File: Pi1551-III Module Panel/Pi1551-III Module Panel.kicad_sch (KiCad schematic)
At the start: 15 parts, among them IC1 OLED, J1 Module Panel, M1 Mounting_Pin, M2 Mounting_Pin, M3 Mounting_Pin, M4 Mounting_Pin, SW1 BACK, SW2 INSERT

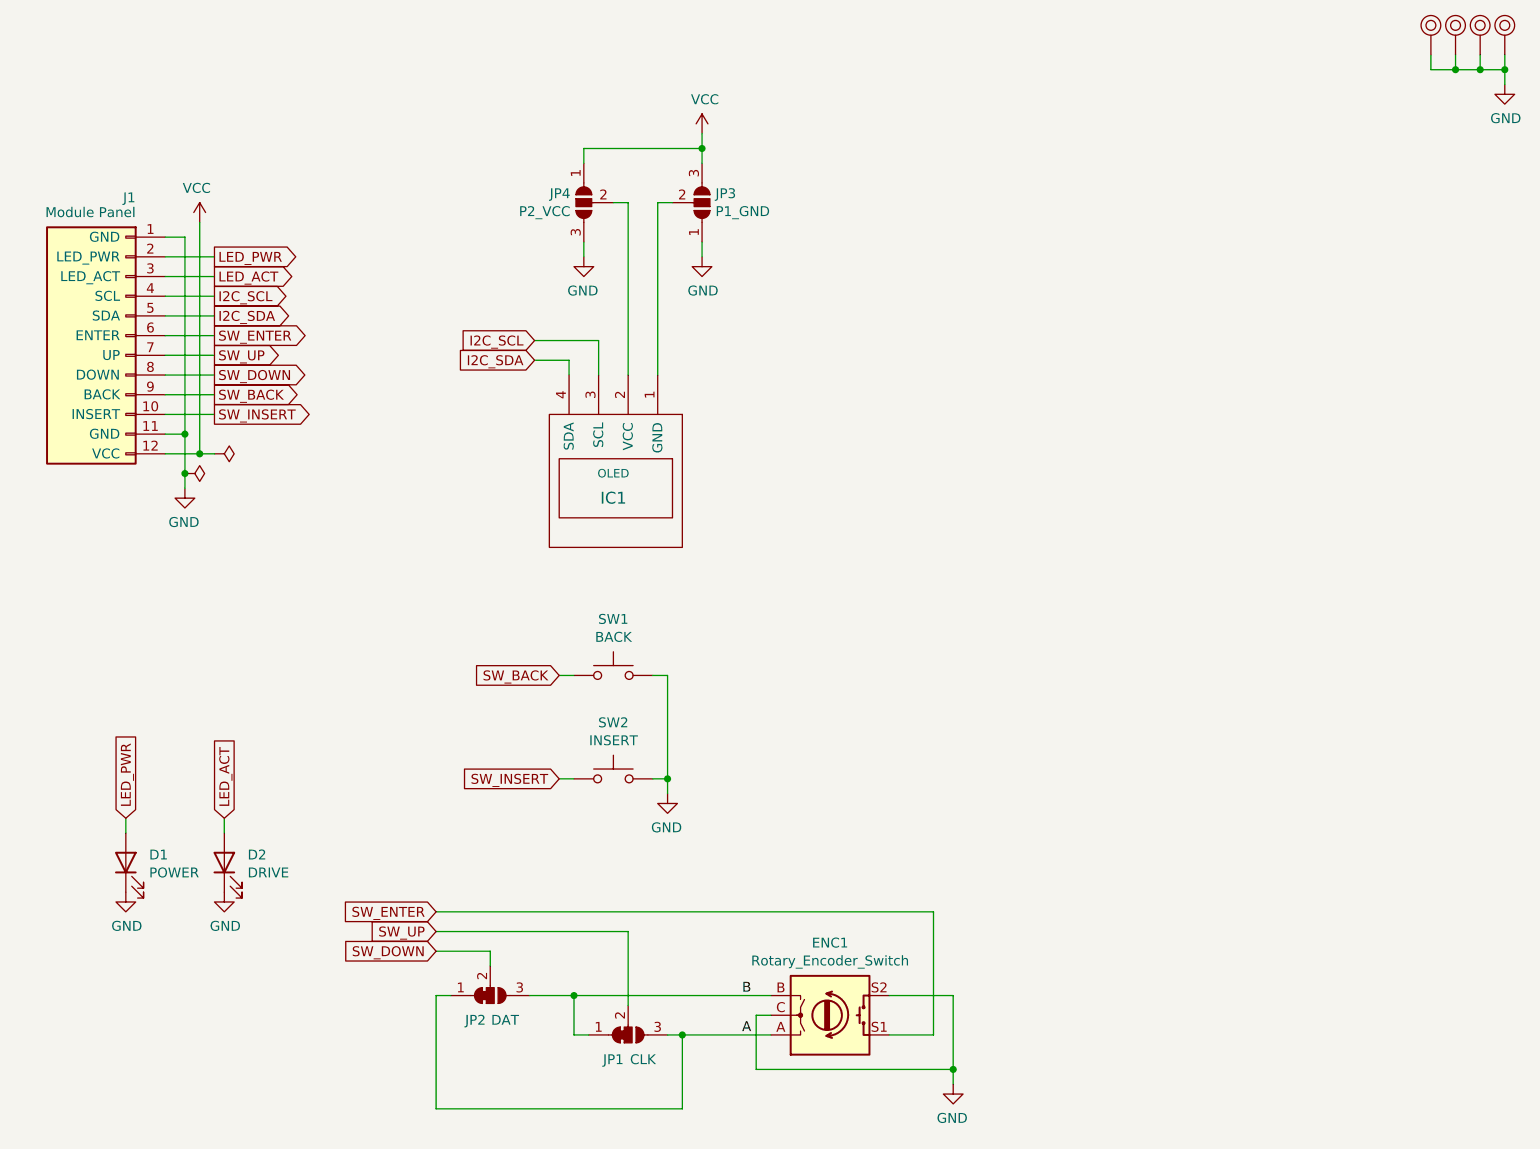
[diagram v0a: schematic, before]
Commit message: PI1551 branding and Microgramma font labels
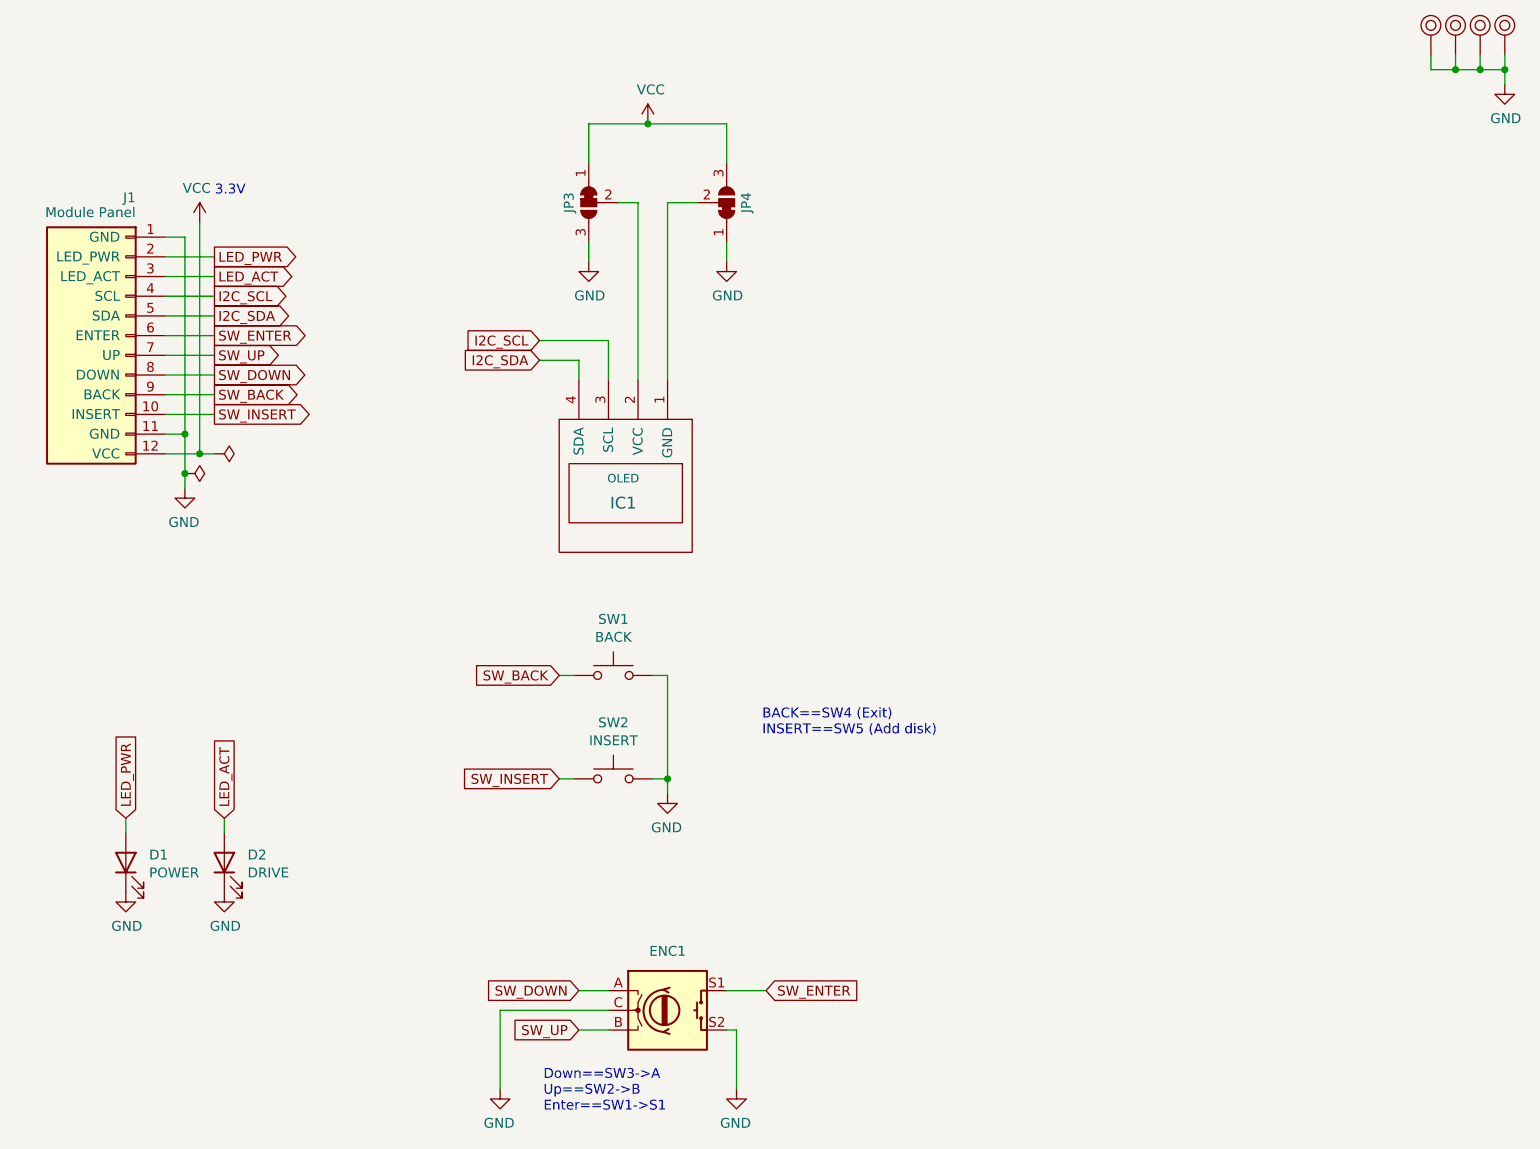
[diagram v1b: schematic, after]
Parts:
- removed ENC1: Rotary_Encoder_Switch, Rotary_Encoder:RotaryEncoder_Alps_EC11E-Switch_Vertical_H20mm, symbol Device:Rotary_Encoder_Switch
- removed JP1: CLK, Jumper:SolderJumper-3_P1.3mm_Open_Pad1.0x1.5mm, symbol Jumper:SolderJumper_3_Bridged12
- removed JP2: DAT, Jumper:SolderJumper-3_P1.3mm_Open_Pad1.0x1.5mm, symbol Jumper:SolderJumper_3_Bridged12
- removed JP3: P1_GND, Jumper:SolderJumper-3_P1.3mm_Open_Pad1.0x1.5mm, symbol I2C_OLED:PowerSelect
- removed JP4: P2_VCC, Jumper:SolderJumper-3_P1.3mm_Open_Pad1.0x1.5mm, symbol I2C_OLED:PowerSelect
- added ENC1: RotaryEncoder_Switch, Rotary_Encoder:RotaryEncoder_Alps_EC11E-Switch_Vertical_H20mm_CircularMountingHoles, symbol Device:RotaryEncoder_Switch
- added JP3, JP4: SolderJumper_3_Bridged12, Jumper:SolderJumper-3_P1.3mm_Bridged12_RoundedPad1.0x1.5mm_NumberLabels, symbol Jumper:SolderJumper_3_Bridged12
- D1, D2, IC1, J1, SW1, SW2: now left out of the parts list
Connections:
- net GND: now also ENC1.C, ENC1.S2, JP3.3 (B), JP4.1 (A)
- net SW_DOWN: now also ENC1.A
- net SW_ENTER: now also ENC1.S1
- net SW_UP: now also ENC1.B
- net VCC: now also JP3.1 (A), JP4.3 (B)
- net at IC1.2 (VCC): now also JP3.2 (C)
- net at IC1.1 (GND): now also JP4.2 (C)
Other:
- note added: "3.3V"
- note added: "BACK==SW4 (Exit) INSERT==SW5 (Add disk)"
- note added: "Down==SW3->A Up==SW2->B Enter==SW1->S1"
- moved on the sheet: IC1

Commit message: gerber files for fabrication
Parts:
- M1, M2, M3, M4: now left out of the parts list
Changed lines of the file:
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@@
 		(unit 1)
 		(exclude_from_sim no)
-		(in_bom yes)
+		(in_bom no)
 		(on_board yes)
 		(dnp no)
@@
 		(unit 1)
 		(exclude_from_sim no)
-		(in_bom yes)
+		(in_bom no)
 		(on_board yes)
 		(dnp no)
@@
 		(unit 1)
 		(exclude_from_sim no)
-		(in_bom yes)
+		(in_bom no)
 		(on_board yes)
 		(dnp no)
@@
 		(unit 1)
 		(exclude_from_sim no)
-		(in_bom yes)
+		(in_bom no)
 		(on_board yes)
 		(dnp no)

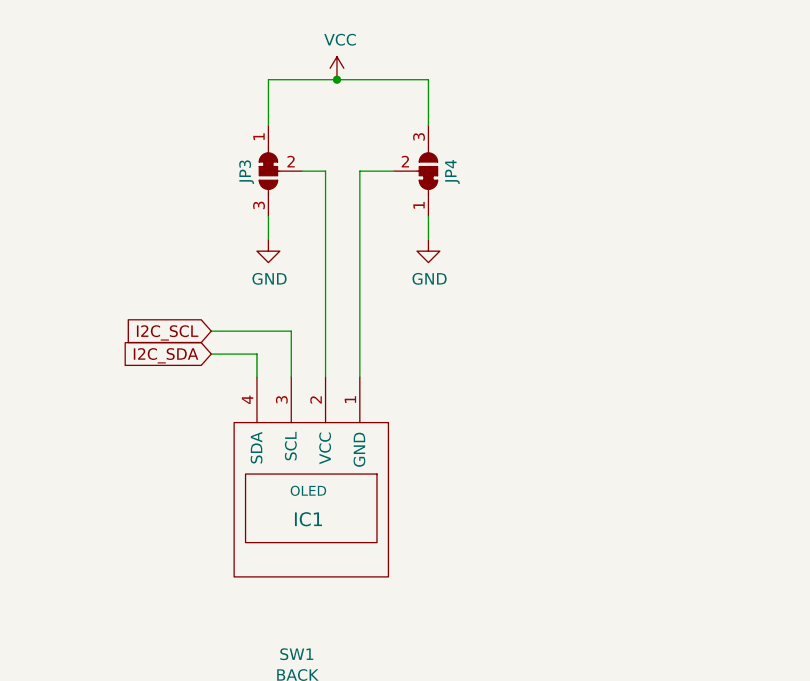
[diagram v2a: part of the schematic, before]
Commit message: change jumpers to be open - it's too difficult to cut them once panel is soldered in
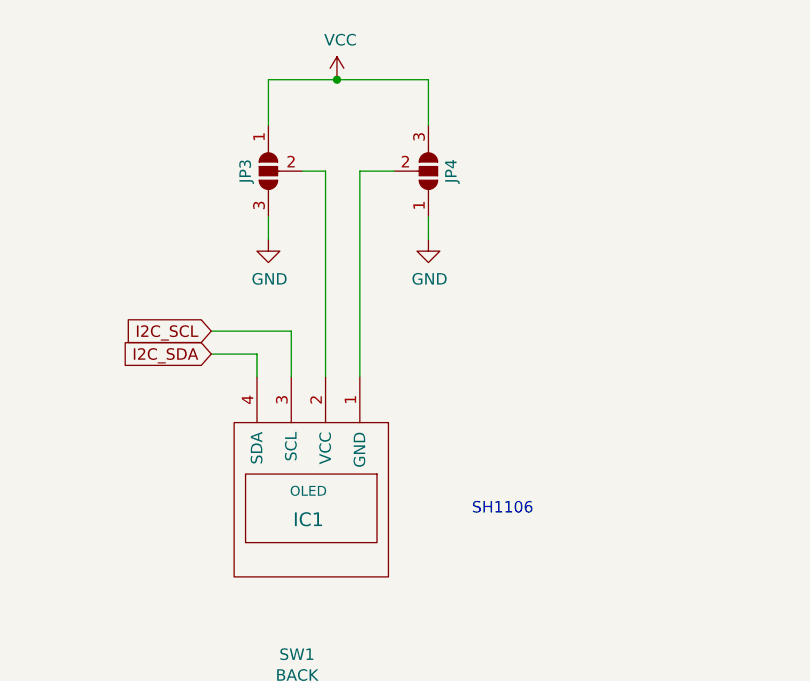
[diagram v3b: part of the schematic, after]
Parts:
- JP3, JP4: value SolderJumper_3_Bridged12 -> SolderJumper_3_Open; footprint Jumper:SolderJumper-3_P1.3mm_Bridged12_RoundedPad1.0x1.5mm_NumberLabels -> Jumper:SolderJumper-3_P1.3mm_Open_RoundedPad1.0x1.5mm_NumberLabels; symbol Jumper:SolderJumper_3_Bridged12 -> Jumper:SolderJumper_3_Open
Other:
- note added: "SH1106"
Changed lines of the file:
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@@
 	(title_block
 		(title "Pi1551-III Module (Panel)")
-		(date "2026-02-02")
-		(rev "1")
+		(date "2026-03-03")
+		(rev "2")
 		(comment 4 "Front panel for the main module, designed for slotting into it.")
 	)
@@
 		(exclude_from_sim no)
 		(at 186.182 105.156 0)
+		(effects
+			(font
+				(size 1.27 1.27)
+			)
+			(justify left)
+		)
+	)
+	(text "SH1106"
+		(exclude_from_sim no)
+		(at 186.436 75.692 0)
 		(effects
 			(font
@@
 	)
 	(symbol
-		(lib_id "Jumper:SolderJumper_3_Bridged12")
+		(lib_id "Jumper:SolderJumper_3_Open")
 		(at 181.61 38.1 270)
 		(mirror x)
@@
 			)
 		)
-		(property "Value" "SolderJumper_3_Bridged12"
+		(property "Value" "SolderJumper_3_Open"
 			(at 185.42 38.1 0)
 			(effects
@@
 			)
 		)
-		(property "Footprint" "Jumper:SolderJumper-3_P1.3mm_Bridged12_RoundedPad1.0x1.5mm_NumberLabels"
+		(property "Footprint" "Jumper:SolderJumper-3_P1.3mm_Open_RoundedPad1.0x1.5mm_NumberLabels"
 			(at 181.61 38.1 0)
 			(effects
@@
 			)
 		)
-		(property "Description" "3-pole Solder Jumper, pins 1+2 closed/bridged"
+		(property "Description" "Solder Jumper, 3-pole, open"
 			(at 181.61 38.1 0)
 			(effects
@@
 	)
 	(symbol
-		(lib_id "Jumper:SolderJumper_3_Bridged12")
+		(lib_id "Jumper:SolderJumper_3_Open")
 		(at 163.83 38.1 90)
 		(mirror x)
@@
 			)
 		)
-		(property "Value" "SolderJumper_3_Bridged12"
+		(property "Value" "SolderJumper_3_Open"
 			(at 160.02 38.1 0)
 			(effects
@@
 			)
 		)
-		(property "Footprint" "Jumper:SolderJumper-3_P1.3mm_Bridged12_RoundedPad1.0x1.5mm_NumberLabels"
+		(property "Footprint" "Jumper:SolderJumper-3_P1.3mm_Open_RoundedPad1.0x1.5mm_NumberLabels"
 			(at 163.83 38.1 0)
 			(effects
@@
 			)
 		)
-		(property "Description" "3-pole Solder Jumper, pins 1+2 closed/bridged"
+		(property "Description" "Solder Jumper, 3-pole, open"
 			(at 163.83 38.1 0)
 			(effects
